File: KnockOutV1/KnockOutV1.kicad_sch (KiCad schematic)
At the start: 1 part, among them U1 STM32F103C8T6

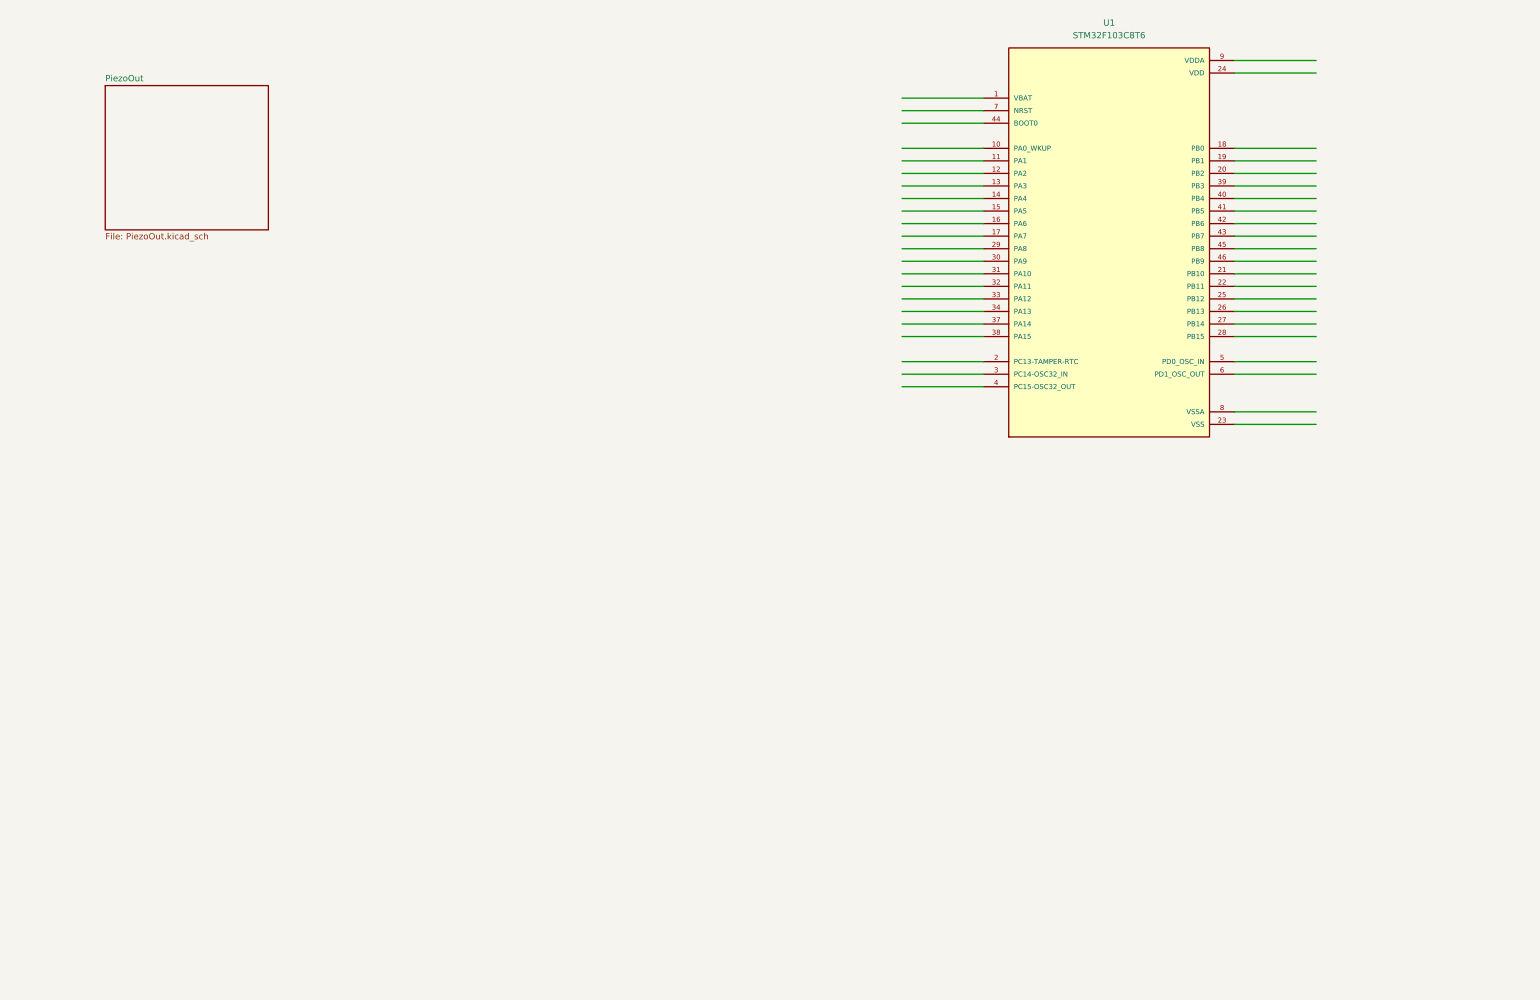
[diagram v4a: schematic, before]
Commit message: Began schematic of KnockOutV1
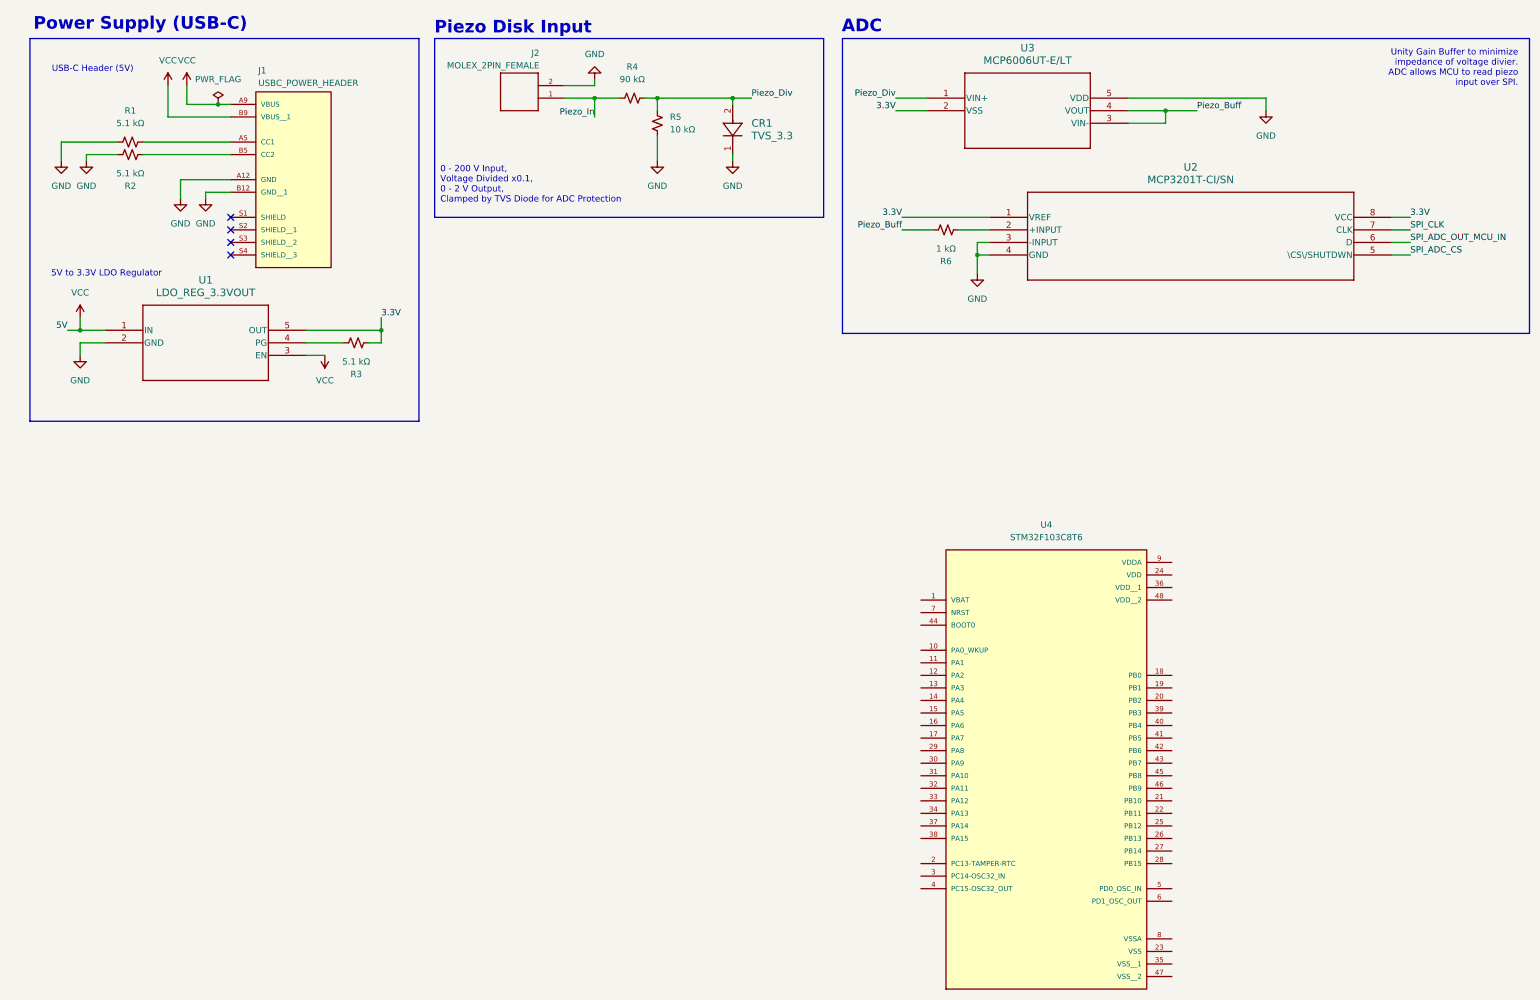
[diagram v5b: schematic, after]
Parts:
- removed U1: STM32F103C8T6, STM32F103C8T6:QFP50P900X900X160-48N, symbol STM32F103C8T6:STM32F103C8T6
- added CR1: TVS_3.3, CR_SOD-123FL_LTF, symbol KnockOutV1_Symbols:SMF3.3
- added J1: USBC_POWER_HEADER, USB4125-GF-A_REVA2:GCT_USB4125-GF-A_REVA2, symbol KnockOutV1_Symbols:USB4125-GF-A_REVA2
- added J2: MOLEX_2PIN_FEMALE, 430450202:CONN_SD-43045-001_02_MOL, symbol KnockOutV1_Symbols:430450202
- added R1, R2, R3: 5.1 kΩ, symbol Device:R_Small_US
- added R4: 90 kΩ, symbol Device:R_Small_US
- added R5: 10 kΩ, symbol Device:R_Small_US
- added R6: 1 kΩ, symbol Device:R_Small_US
- added U1: LDO_REG_3.3VOUT, FP-NCP164CSN330T1G_OSI, symbol KnockOutV1_Symbols:NCP164CSN330T1G
- added U2: MCP3201T-CI/SN, SOIC8-N_MC_MCH, symbol KnockOutV1_Symbols:MCP3201T-CI_SN
- added U3: MCP6006UT-E/LT, SC70-5_LT_MCH, symbol KnockOutV1_Symbols:MCP6006UT-E_LT
- added U4: STM32F103C8T6, STM32F103C8T6:QFP50P900X900X160-48N, symbol KnockOutV1_Symbols:STM32F103C8T6
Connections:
- new net: J1.A5 (CC1), R1.2
- new net: J1.B5 (CC2), R2.2
- new net: R6.1, U2.2 (+INPUT)
- new net: R3.2, U1.4 (PG)
- new net 3.3V: R3.1, U1.5 (OUT), U2.1 (VREF), U2.8 (VCC), U3.2 (VSS)
- new net GND: CR1.1, J1.A12 (GND), J1.B12 (GND__1), J2.2, R1.1, R2.1, R5.2, U1.2 (GND), U2.3 (-INPUT), U2.4 (GND), U3.5 (VDD)
- new net Piezo_Buff: R6.2, U3.3 (VIN-), U3.4 (VOUT)
- new net Piezo_Div: CR1.2, R4.2, R5.1, U3.1 (VIN+)
- new net Piezo_In: J2.1, R4.1
- new net SPI_ADC_CS: U2.5 (\CS\/SHUTDWN)
- new net SPI_ADC_OUT_MCU_IN: U2.6 (D)
- new net SPI_CLK: U2.7 (CLK)
- new net VCC: J1.A9 (VBUS), J1.B9 (VBUS__1), U1.1 (IN), U1.3 (EN)
- no-connect marks 0 -> 4
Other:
- removed sheet PiezoOut
- note added: "0 - 200 V Input, Voltage Divided x0.1, 0 - 2 V Output, Clamped by TVS Diode for ADC Protection"
- note added: "5V to 3.3V LDO Regulator"
- note added: "ADC"
- note added: "Piezo Disk Input"
- note added: "Power Supply (USB-C)"
- note added: "USB-C Header (5V)"
- note added: "Unity Gain Buffer to minimize impedance of voltage divier. ADC allows MCU to read piezo input over SPI."
